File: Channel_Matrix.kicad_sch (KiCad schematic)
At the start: 16 parts, among them U2301 LP38690SDX-3.3/NOPB

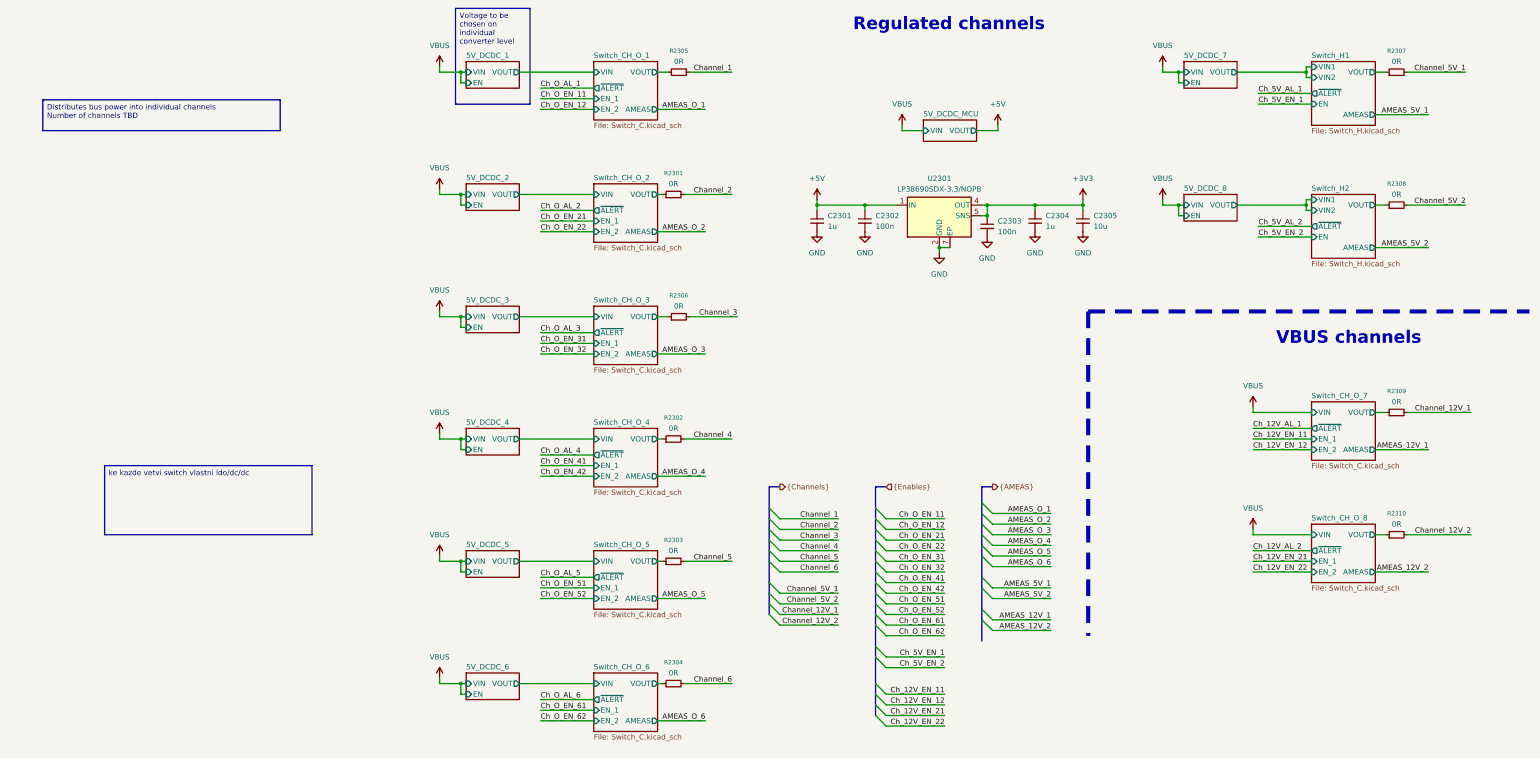
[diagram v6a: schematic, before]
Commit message: added RS422, housekeeping
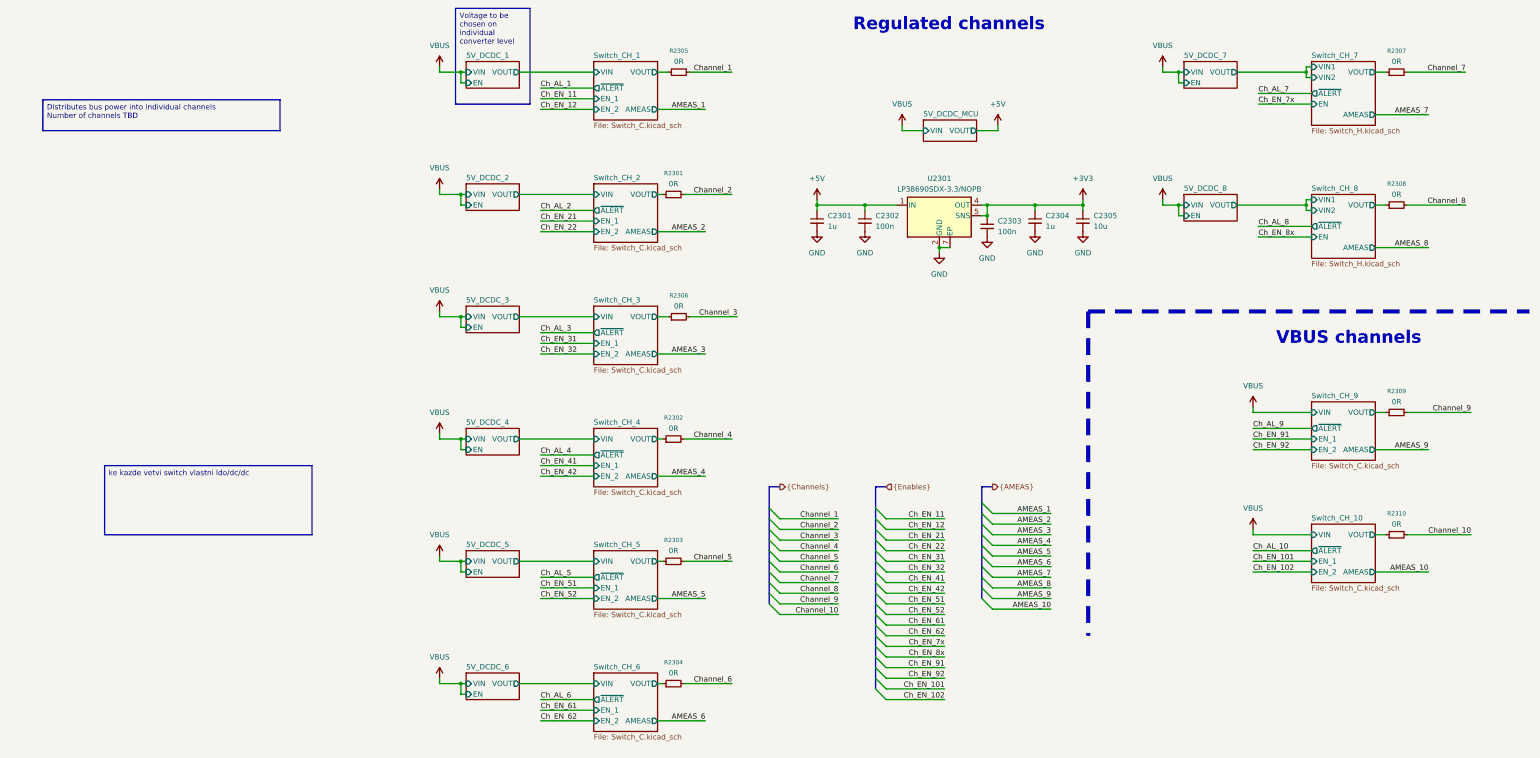
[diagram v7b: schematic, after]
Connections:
- net Channel_12V_1 renamed Channel_9
- net Channel_12V_2 renamed Channel_10
- net Channel_5V_1 renamed Channel_7
- net Channel_5V_2 renamed Channel_8
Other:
- sheet Switch_CH_O_1 renamed Switch_CH_1
- sheet Switch_CH_O_2 renamed Switch_CH_2
- sheet Switch_CH_O_3 renamed Switch_CH_3
- sheet Switch_CH_O_4 renamed Switch_CH_4
- sheet Switch_CH_O_5 renamed Switch_CH_5
- sheet Switch_CH_O_6 renamed Switch_CH_6
- sheet Switch_CH_O_7 renamed Switch_CH_9
- sheet Switch_CH_O_8 renamed Switch_CH_10
- sheet Switch_H1 renamed Switch_CH_7
- sheet Switch_H2 renamed Switch_CH_8

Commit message: updated battery pack module; updated solar inputs module
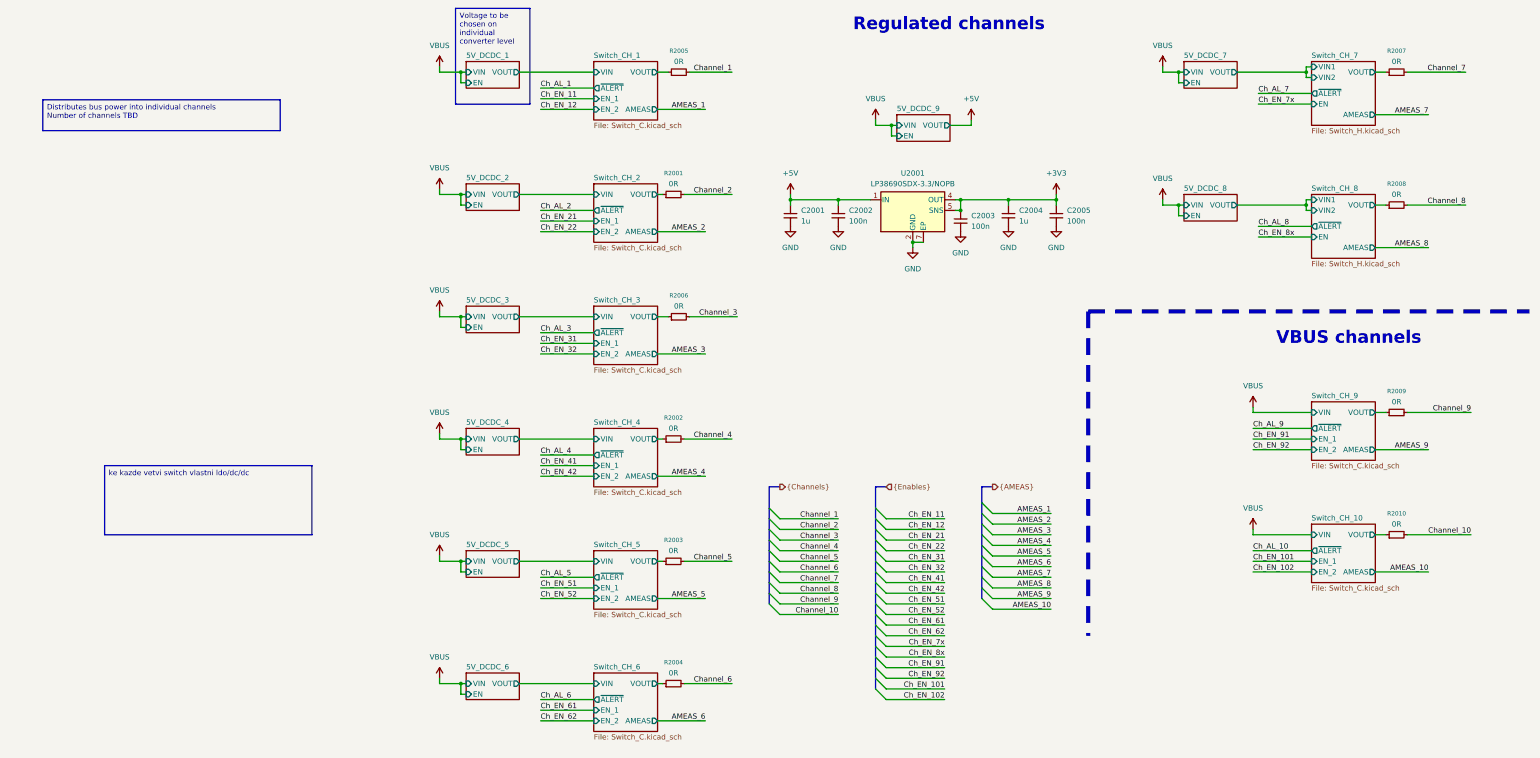
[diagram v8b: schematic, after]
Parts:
- removed C2305: 10u, Capacitor_SMD:C_0603_1608Metric_Pad1.08x0.95mm_HandSolder, symbol Device:C_Small
- added C2005: 100n, Capacitor_SMD:C_0603_1608Metric_Pad1.08x0.95mm_HandSolder, symbol Device:C_Small
- renumbered C2301 to C2001, C2302 to C2002, C2303 to C2003, C2304 to C2004, R2301 to R2001, R2302 to R2002, R2303 to R2003, R2304 to R2004, R2305 to R2005, R2306 to R2006, R2307 to R2007, R2308 to R2008, R2309 to R2009, R2310 to R2010, U2301 to U2001
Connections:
- net +3V3: now also C2005.1
- net GND: now also C2005.2
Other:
- removed sheet 5V_DCDC_MCU
- added sheet 5V_DCDC_9 (LDO_5V.kicad_sch)
- moved on the sheet: C2001, C2002, C2003, C2004, U2001
